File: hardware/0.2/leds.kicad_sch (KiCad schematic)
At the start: 16 parts, among them Q2 BSS138, Q3 BSS138, Q4 BSS138

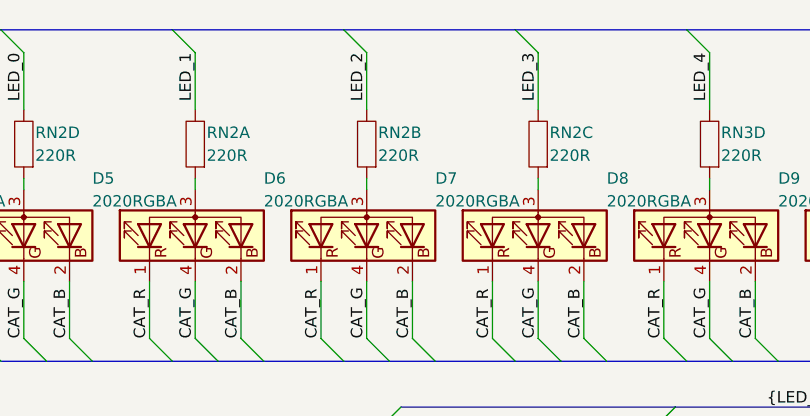
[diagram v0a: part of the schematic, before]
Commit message: half IO routed out
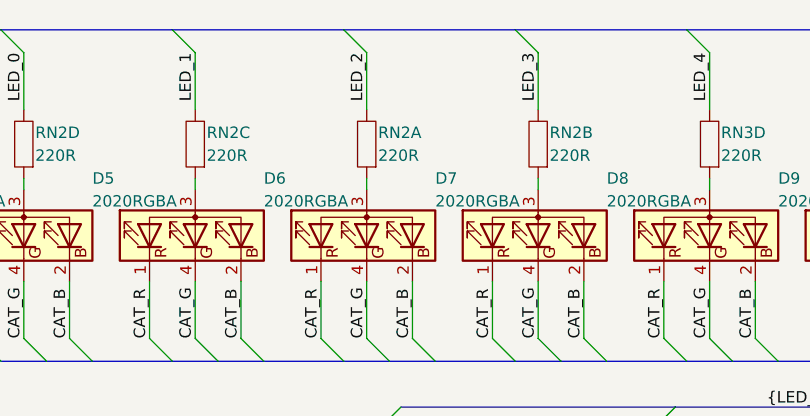
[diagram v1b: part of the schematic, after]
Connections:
- net LED_1: now also RN2.7; no longer RN2.5
- net LED_2: now also RN2.5; no longer RN2.6
- net LED_3: now also RN2.6; no longer RN2.7
- net at RN2.2: now also D5.3 (A); no longer D7.3 (A)
- net at RN2.4: now also D6.3 (A); no longer D5.3 (A)
- net at RN2.3: now also D7.3 (A); no longer D6.3 (A)
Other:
- moved on the sheet: RN2A, RN2B, RN2C
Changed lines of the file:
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@@
     )
   )
-  (symbol (lib_id "josh-passive:RN") (at 111.76 82.55 90) (unit 1)
+  (symbol (lib_id "josh-passive:RN") (at 111.76 82.55 90) (unit 3)
     (in_bom yes) (on_board yes)
     (property "Reference" "RN2" (id 0) (at 113.03 81.28 90)
@@
     )
   )
-  (symbol (lib_id "josh-passive:RN") (at 130.81 82.55 90) (unit 2)
+  (symbol (lib_id "josh-passive:RN") (at 130.81 82.55 90) (unit 1)
     (in_bom yes) (on_board yes)
     (property "Reference" "RN2" (id 0) (at 132.08 81.28 90)
@@
     )
   )
-  (symbol (lib_id "josh-passive:RN") (at 149.86 82.55 90) (unit 3)
+  (symbol (lib_id "josh-passive:RN") (at 149.86 82.55 90) (unit 2)
     (in_bom yes) (on_board yes)
     (property "Reference" "RN2" (id 0) (at 151.13 81.28 90)

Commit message: almost there
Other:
- note added: "LEDs"
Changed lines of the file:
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@@
     (stroke (width 0) (type solid) (color 0 0 0 0))
+  )
+  (text "LEDs" (at 155.575 50.8 180)
+    (effects (font (size 5 5)) (justify right bottom))
   )
   (label "CAT_R" (at 87.63 104.14 90)

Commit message: shipped 0.2
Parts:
- Q501: renamed from Q2; MPN2 (none) -> BSS138W-7-F; Manufacturer2 (none) -> Diodes Incorporated
- Q502: renamed from Q3; MPN2 (none) -> BSS138W-7-F; Manufacturer2 (none) -> Diodes Incorporated
- Q503: renamed from Q4; MPN2 (none) -> BSS138W-7-F; Manufacturer2 (none) -> Diodes Incorporated
- R510: renamed from R25; LCSC C25531 -> C60489; MPN 0402WGJ0103TCE -> RC0402JR-0710KL; MPN2 (none) -> 0402WGJ0103TCE; Manufacturer UNI-ROYAL(Uniroyal Elec) -> Yageo; Manufacturer2 (none) -> UNI-ROYAL(Uniroyal Elec)
- R513: renamed from R30; LCSC C25531 -> C60489; MPN 0402WGJ0103TCE -> RC0402JR-0710KL; MPN2 (none) -> 0402WGJ0103TCE; Manufacturer UNI-ROYAL(Uniroyal Elec) -> Yageo; Manufacturer2 (none) -> UNI-ROYAL(Uniroyal Elec)
- R515: renamed from R28; LCSC C25531 -> C60489; MPN 0402WGJ0103TCE -> RC0402JR-0710KL; MPN2 (none) -> 0402WGJ0103TCE; Manufacturer UNI-ROYAL(Uniroyal Elec) -> Yageo; Manufacturer2 (none) -> UNI-ROYAL(Uniroyal Elec)
- RN500: renamed from RN3; LCSC C25498 -> C706474; MPN 4D02WGJ0221TCE -> YC164-JR-07220RL; MPN2 (none) -> 4D02WGJ0221TCE; Manufacturer UNI-ROYAL(Uniroyal Elec) -> Yageo; Manufacturer2 (none) -> UNI-ROYAL(Uniroyal Elec)
- RN501: renamed from RN2; LCSC C25498 -> C706474; MPN 4D02WGJ0221TCE -> YC164-JR-07220RL; MPN2 (none) -> 4D02WGJ0221TCE; Manufacturer UNI-ROYAL(Uniroyal Elec) -> Yageo; Manufacturer2 (none) -> UNI-ROYAL(Uniroyal Elec)
- renumbered D11 to D1, D10 to D2, D9 to D3, D8 to D4, D7 to D5, D5 to D7, D4 to D8

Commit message: checking for the final time
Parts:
- R510, R513, R515: MPN RC0402JR-0710KL -> RC0402JR-0710KL
- RN500, RN501: MPN YC164-JR-07220RL -> YC124-JR-07220RL
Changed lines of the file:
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@@
       (effects (font (size 1.27 1.27)) hide)
     )
-    (property "MPN" "YC164-JR-07220RL" (id 5) (at 92.71 82.55 0)
+    (property "MPN" "YC124-JR-07220RL\n" (id 5) (at 92.71 82.55 0)
       (effects (font (size 1.27 1.27)) hide)
     )
@@
       (effects (font (size 1.27 1.27)) hide)
     )
-    (property "MPN" "YC164-JR-07220RL" (id 5) (at 111.76 82.55 0)
+    (property "MPN" "YC124-JR-07220RL\n" (id 5) (at 111.76 82.55 0)
       (effects (font (size 1.27 1.27)) hide)
     )
@@
       (effects (font (size 1.27 1.27)) hide)
     )
-    (property "MPN" "YC164-JR-07220RL" (id 5) (at 130.81 82.55 0)
+    (property "MPN" "YC124-JR-07220RL\n" (id 5) (at 130.81 82.55 0)
       (effects (font (size 1.27 1.27)) hide)
     )
@@
       (effects (font (size 1.27 1.27)) hide)
     )
-    (property "MPN" "YC164-JR-07220RL" (id 5) (at 149.86 82.55 0)
+    (property "MPN" "YC124-JR-07220RL\n" (id 5) (at 149.86 82.55 0)
       (effects (font (size 1.27 1.27)) hide)
     )
@@
       (effects (font (size 1.27 1.27)) hide)
     )
-    (property "MPN" "YC164-JR-07220RL" (id 5) (at 168.91 82.55 0)
+    (property "MPN" "YC124-JR-07220RL\n" (id 5) (at 168.91 82.55 0)
       (effects (font (size 1.27 1.27)) hide)
     )
@@
       (effects (font (size 1.27 1.27)) hide)
     )
-    (property "MPN" "YC164-JR-07220RL" (id 5) (at 187.96 82.55 0)
+    (property "MPN" "YC124-JR-07220RL\n" (id 5) (at 187.96 82.55 0)
       (effects (font (size 1.27 1.27)) hide)
     )
@@
       (effects (font (size 1.27 1.27)) hide)
     )
-    (property "MPN" "YC164-JR-07220RL" (id 5) (at 207.01 82.55 0)
+    (property "MPN" "YC124-JR-07220RL\n" (id 5) (at 207.01 82.55 0)
       (effects (font (size 1.27 1.27)) hide)
     )
@@
       (effects (font (size 1.27 1.27)) hide)
     )
-    (property "MPN" "YC164-JR-07220RL" (id 5) (at 226.06 82.55 0)
+    (property "MPN" "YC124-JR-07220RL\n" (id 5) (at 226.06 82.55 0)
       (effects (font (size 1.27 1.27)) hide)
     )
@@
       (effects (font (size 1.27 1.27)) hide)
     )
-    (property "MPN" "RC0402JR-0710KL" (id 5) (at 123.19 130.81 0)
+    (property "MPN" "RC0402JR-0710KL\n" (id 5) (at 123.19 130.81 0)
       (effects (font (size 1.27 1.27)) hide)
     )
@@
       (effects (font (size 1.27 1.27)) hide)
     )
-    (property "MPN" "RC0402JR-0710KL" (id 5) (at 153.67 130.81 0)
+    (property "MPN" "RC0402JR-0710KL\n" (id 5) (at 153.67 130.81 0)
       (effects (font (size 1.27 1.27)) hide)
     )
@@
       (effects (font (size 1.27 1.27)) hide)
     )
-    (property "MPN" "RC0402JR-0710KL" (id 5) (at 181.61 130.81 0)
-      (effects (font (size 1.27 1.27)) hide)
-    )
+    (property "MPN" "RC0402JR-0710KL\n" (id 5) (at 181.61 130.81 0)
+      (effects (font (size 1.27 1.27)) hide)
+    )

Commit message: nightly version bump
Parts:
- Q501, Q502, Q503: MPN2 BSS138W-7-F -> (none)
- R510, R513, R515: MPN2 0402WGJ0103TCE -> (none)
- RN500, RN501: MPN2 4D02WGJ0221TCE -> (none)
